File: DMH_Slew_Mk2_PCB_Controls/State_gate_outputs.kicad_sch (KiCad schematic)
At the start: 25 parts, among them J4 TS_Jack_6.35mm_Sw, J5 TS_Jack_6.35mm_Sw, Q5 BC548, Q6 BC548, U1 TL074

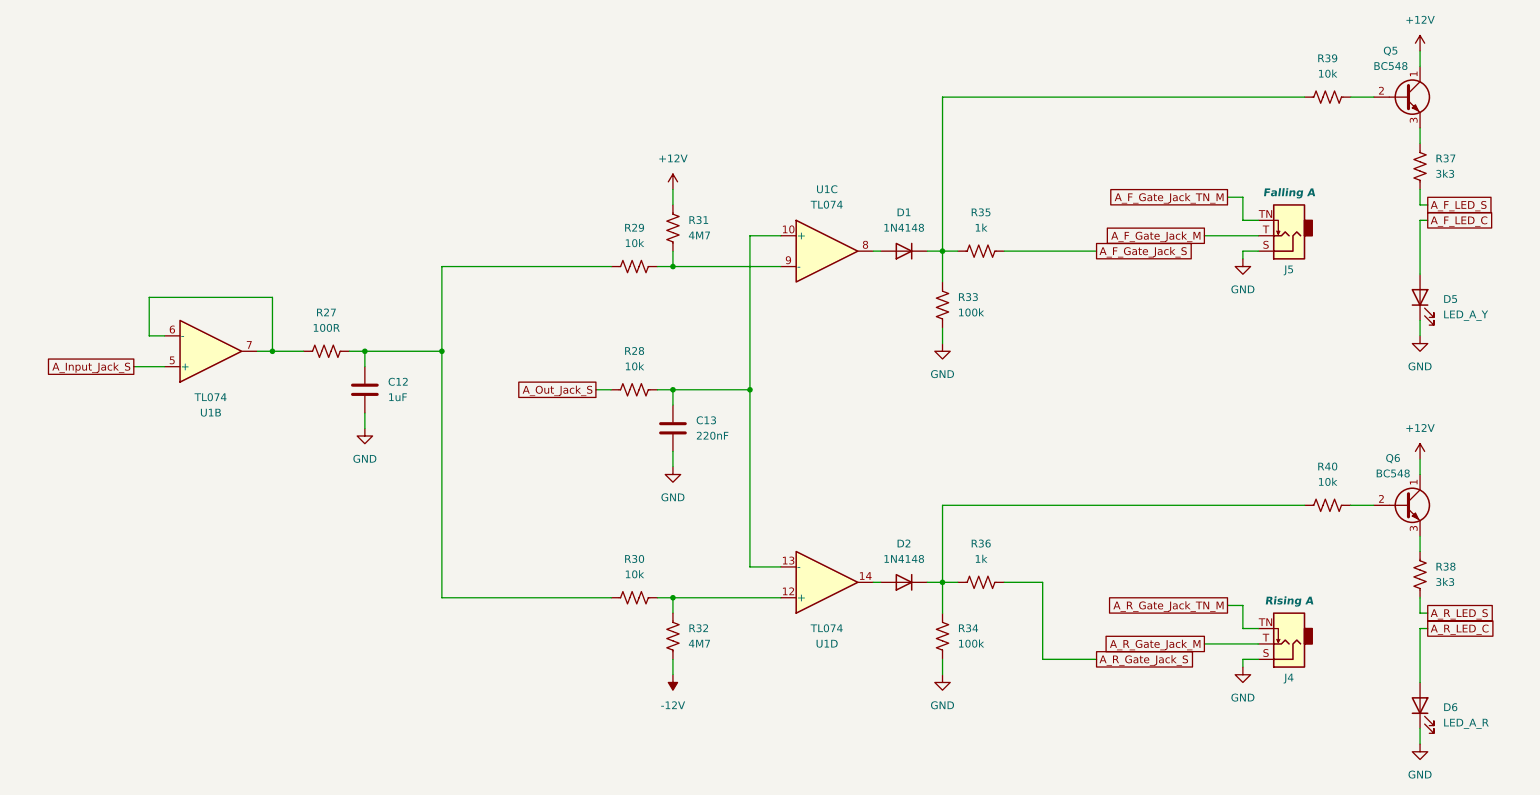
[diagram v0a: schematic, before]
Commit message: Designed Controls PCB
... and removed Mod feature
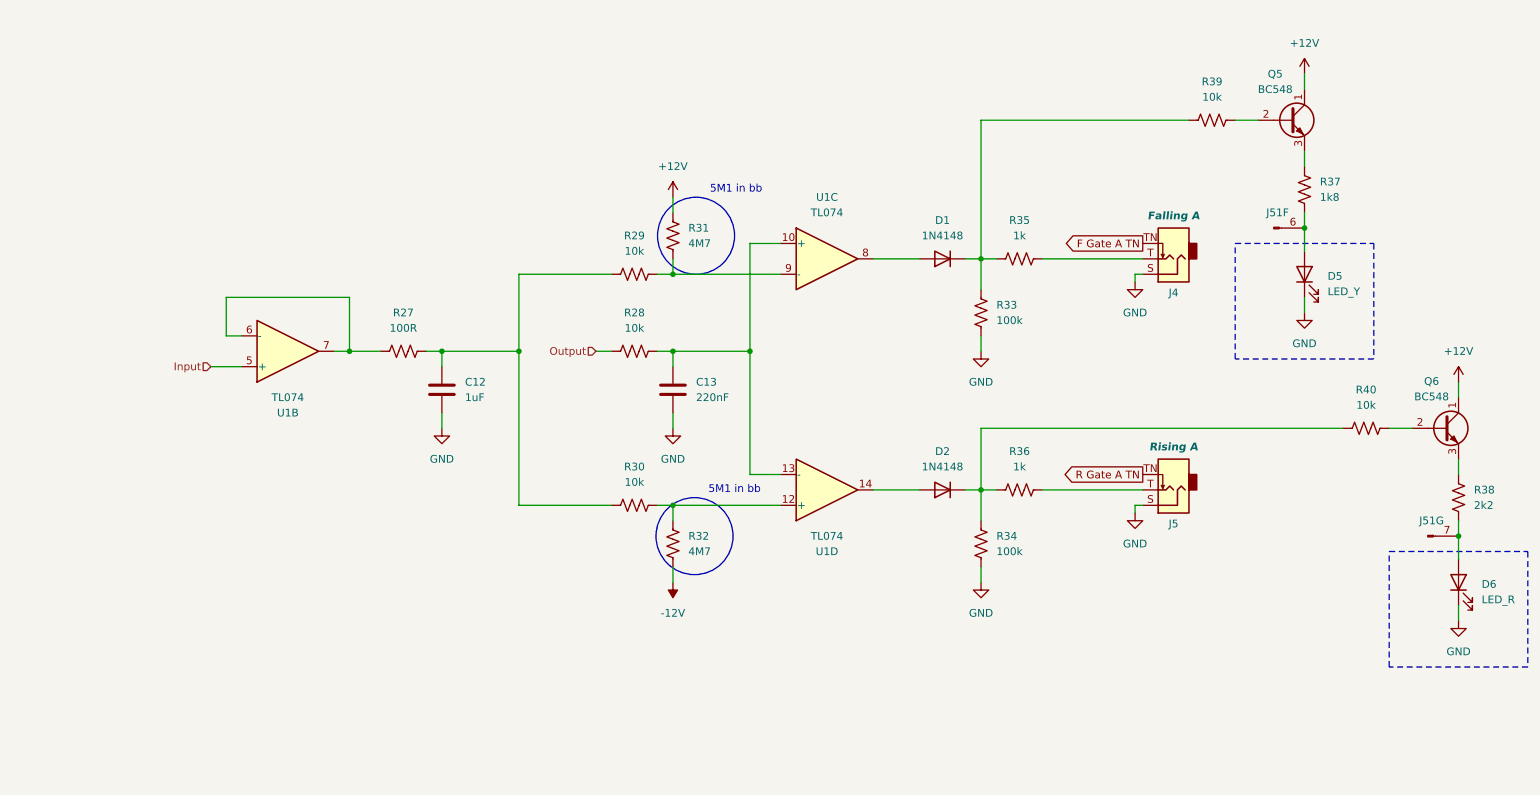
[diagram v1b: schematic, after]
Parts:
- added J51: Conn_01x08_PinHeader, Connector_PinHeader_2.54mm:PinHeader_1x08_P2.54mm_Vertical, symbol SynthStuff:Conn_01x08_PinHeader
- D5: value LED_A_Y -> LED_Y
- D6: value LED_A_R -> LED_R
- Q5: footprint Package_TO_SOT_THT:TO-92_Inline -> Package_TO_SOT_THT:TO-92L_Inline_Wide
- R37: value 3k3 -> 1k8
- R38: value 3k3 -> 2k2
- U1: footprint Package_DIP:DIP-14_W7.62mm_Socket -> Package_DIP:DIP-16_W7.62mm_Socket
- renumbered J5 to J4, J4 to J5
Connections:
- net A_F_Gate_Jack_S is gone; now on an unnamed net: R35.1
- net A_F_LED_S is gone; now on an unnamed net: R37.2
- net A_R_Gate_Jack_S is gone; now on an unnamed net: R36.1
- net A_R_LED_S is gone; now on an unnamed net: R38.2
- net A_F_Gate_Jack_M: no longer names the net of J4.T
- net A_F_Gate_Jack_TN_M renamed F Gate A TN
- net A_F_LED_C: no longer names the net of D5.2 (A)
- net A_F_LED_C: now also J51.6 (Pin_6)
- net A_Input_Jack_S renamed Input
- net A_Out_Jack_S renamed Output
- net A_R_Gate_Jack_M: no longer names the net of J5.T
- net A_R_Gate_Jack_TN_M renamed R Gate A TN
- net A_R_LED_C: no longer names the net of D6.2 (A)
- net A_R_LED_C: now also J51.7 (Pin_7)
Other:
- note added: "5M1 in bb"
- moved on the sheet: C12, C13, D1, D2, D5, D6, J4, J5, Q5, Q6, R27, R28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
